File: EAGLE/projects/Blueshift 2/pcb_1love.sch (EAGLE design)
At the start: 20 parts, among them X1 RASPI_BOARD_B+_F

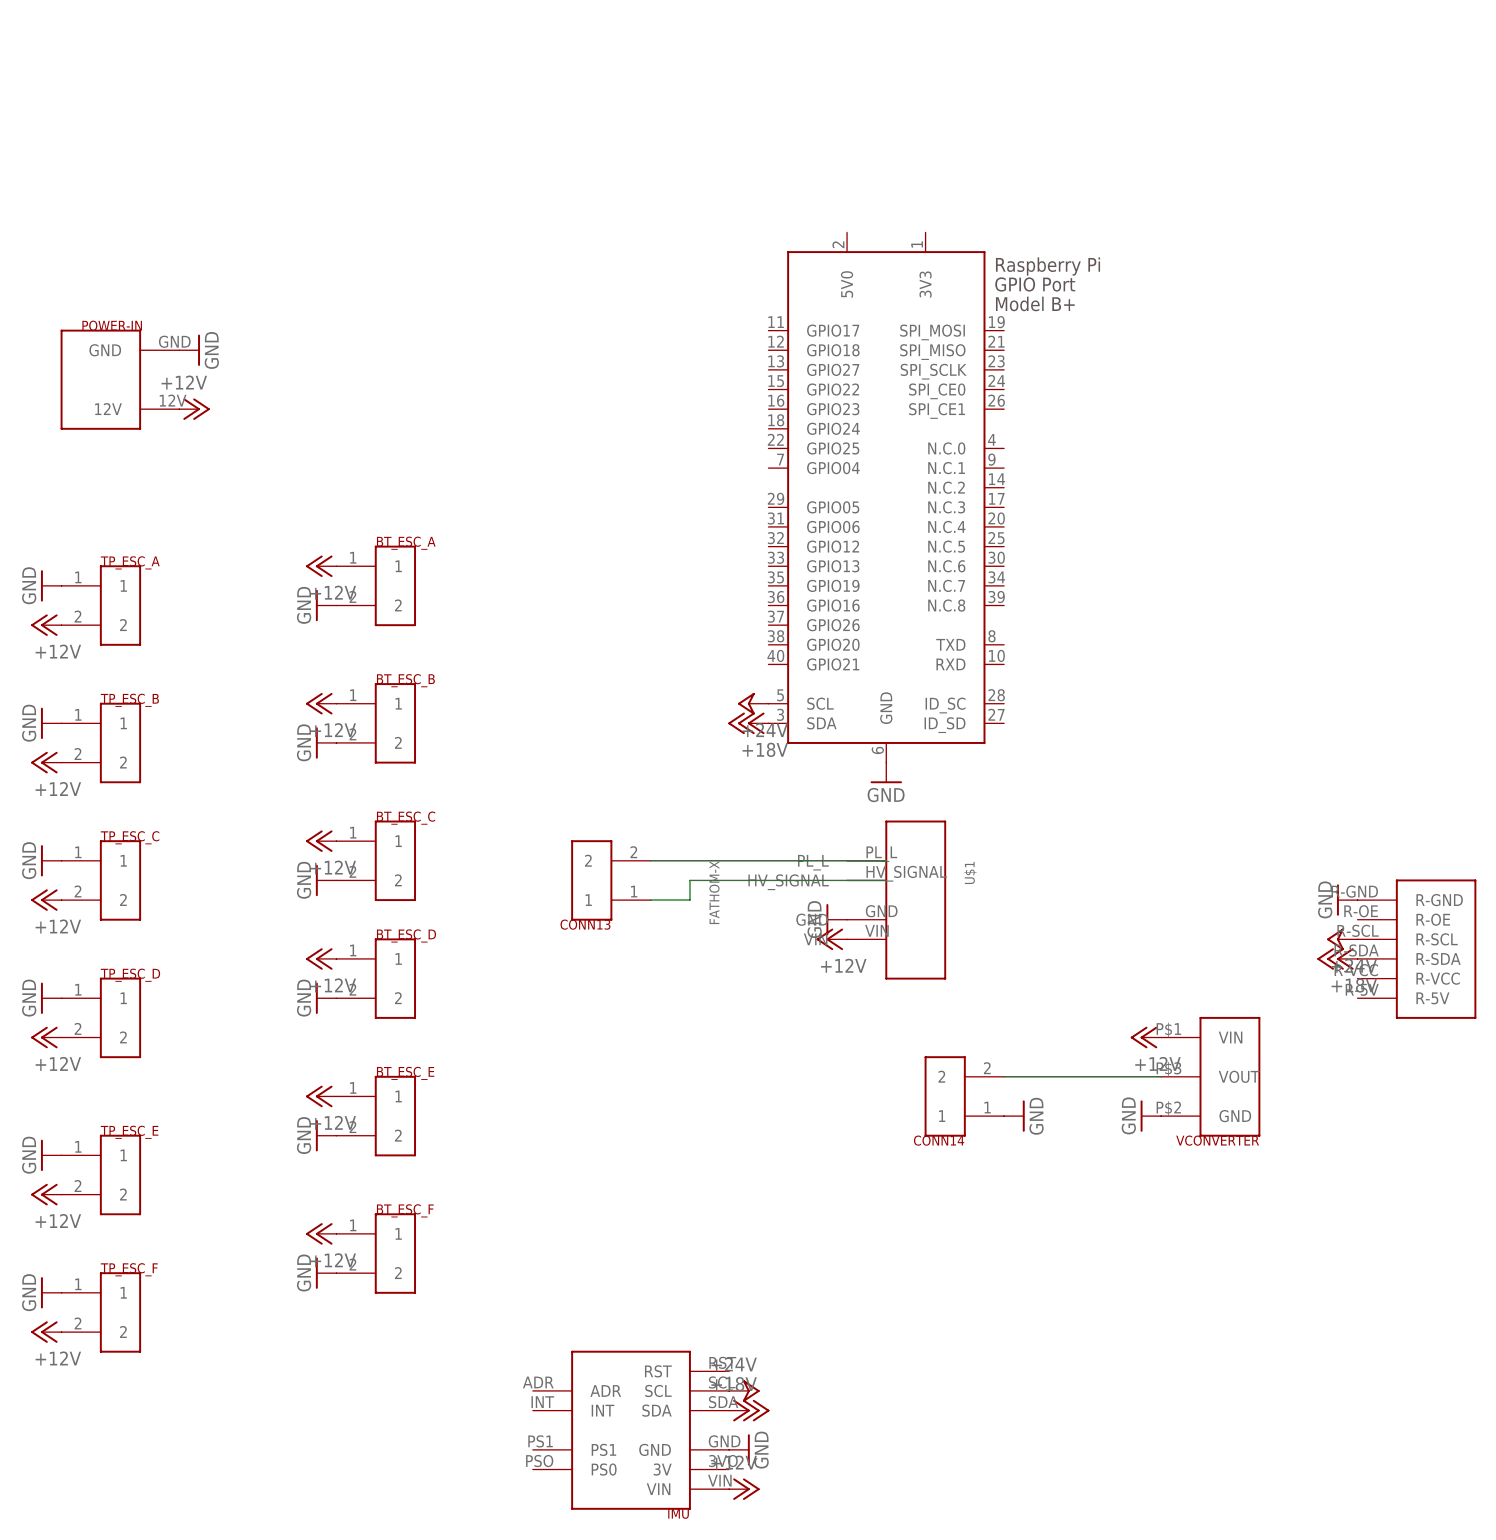
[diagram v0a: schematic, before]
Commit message: Fix power to IMU and PWM, RasPi cutout
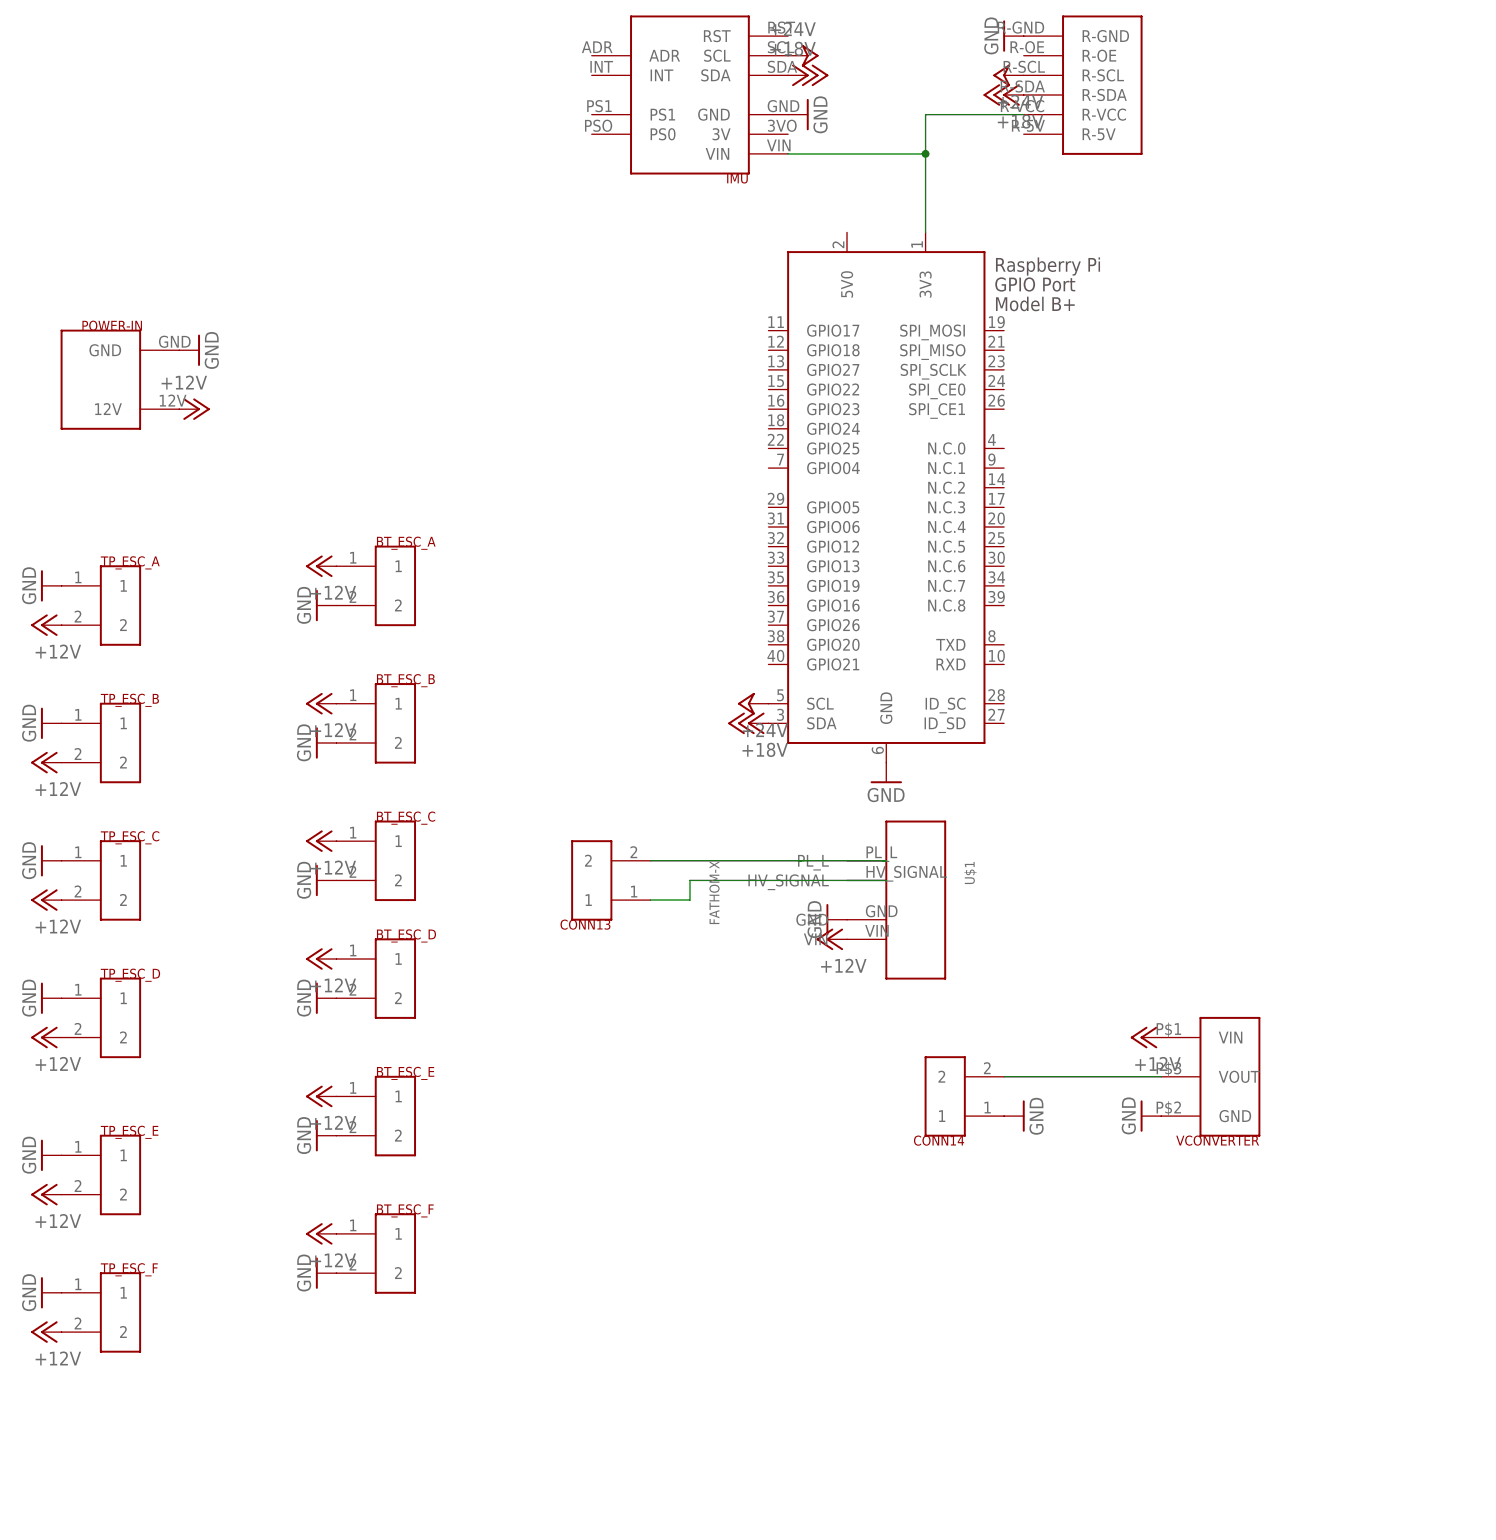
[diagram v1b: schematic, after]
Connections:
- new net N$4: IMU.VIN, PWM_EXT.R-VCC, X1.3V3
- net +12V: no longer IMU.VIN
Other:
- moved on the sheet: IMU
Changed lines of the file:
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@@
 <?xml version="1.0" encoding="utf-8"?>
 <!DOCTYPE eagle SYSTEM "eagle.dtd">
-<eagle version="9.5.2">
+<eagle version="9.6.0">
 <drawing>
 <settings>
@@
 <part name="GND18" library="supply1" library_urn="urn:adsk.eagle:library:371" deviceset="GND" device=""/>
 <part name="CONN14" library="BlueShift" deviceset="2CONTACT_ULTRAFIT_R/A" device=""/>
-<part name="P+20" library="supply1" library_urn="urn:adsk.eagle:library:371" deviceset="+12V" device=""/>
 <part name="GND19" library="supply1" library_urn="urn:adsk.eagle:library:371" deviceset="GND" device=""/>
 <part name="P+21" library="supply1" library_urn="urn:adsk.eagle:library:371" deviceset="+12V" device=""/>
@@
 </plain>
 <instances>
-<instance part="PWM_EXT" gate="G$1" x="106.68" y="55.88" smashed="yes"/>
-<instance part="IMU" gate="G$1" x="0" y="0" smashed="yes" rot="R180">
-<attribute name="NAME" x="7.62" y="-10.16" size="1.27" layer="94" rot="R180"/>
-<attribute name="VALUE" x="-7.62" y="10.16" size="1.27" layer="94"/>
+<instance part="PWM_EXT" gate="G$1" x="63.5" y="167.64" smashed="yes"/>
+<instance part="IMU" gate="G$1" x="7.62" y="172.72" smashed="yes" rot="R180">
+<attribute name="NAME" x="15.24" y="162.56" size="1.27" layer="94" rot="R180"/>
+<attribute name="VALUE" x="0" y="182.88" size="1.27" layer="94"/>
 </instance>
 <instance part="VCONVERTER" gate="G$1" x="78.74" y="45.72" smashed="yes">
@@
 <attribute name="VALUE" x="30.48" y="81.28" size="1.778" layer="96"/>
 </instance>
-<instance part="P+14" gate="1" x="15.24" y="5.08" smashed="yes" rot="R270">
-<attribute name="VALUE" x="10.16" y="7.62" size="1.778" layer="96"/>
+<instance part="P+14" gate="1" x="22.86" y="177.8" smashed="yes" rot="R270">
+<attribute name="VALUE" x="17.78" y="180.34" size="1.778" layer="96"/>
 </instance>
 <instance part="P+15" gate="1" x="15.24" y="93.98" smashed="yes" rot="R90">
 <attribute name="VALUE" x="20.32" y="91.44" size="1.778" layer="96" rot="R180"/>
 </instance>
-<instance part="P+16" gate="1" x="91.44" y="63.5" smashed="yes" rot="R90">
-<attribute name="VALUE" x="96.52" y="60.96" size="1.778" layer="96" rot="R180"/>
+<instance part="P+16" gate="1" x="48.26" y="175.26" smashed="yes" rot="R90">
+<attribute name="VALUE" x="53.34" y="172.72" size="1.778" layer="96" rot="R180"/>
 </instance>
 <instance part="P+17" gate="1" x="15.24" y="91.44" smashed="yes" rot="R90">
 <attribute name="VALUE" x="20.32" y="88.9" size="1.778" layer="96" rot="R180"/>
 </instance>
-<instance part="P+18" gate="1" x="15.24" y="2.54" smashed="yes" rot="R270">
-<attribute name="VALUE" x="10.16" y="5.08" size="1.778" layer="96"/>
-</instance>
-<instance part="P+19" gate="1" x="91.44" y="60.96" smashed="yes" rot="R90">
-<attribute name="VALUE" x="96.52" y="58.42" size="1.778" layer="96" rot="R180"/>
-</instance>
-<instance part="GND17" gate="1" x="15.24" y="-2.54" smashed="yes" rot="R90">
-<attribute name="VALUE" x="17.78" y="-5.08" size="1.778" layer="96" rot="R90"/>
-</instance>
-<instance part="GND18" gate="1" x="91.44" y="68.58" smashed="yes" rot="R270">
-<attribute name="VALUE" x="88.9" y="71.12" size="1.778" layer="96" rot="R270"/>
+<instance part="P+18" gate="1" x="22.86" y="175.26" smashed="yes" rot="R270">
+<attribute name="VALUE" x="17.78" y="177.8" size="1.778" layer="96"/>
+</instance>
+<instance part="P+19" gate="1" x="48.26" y="172.72" smashed="yes" rot="R90">
+<attribute name="VALUE" x="53.34" y="170.18" size="1.778" layer="96" rot="R180"/>
+</instance>
+<instance part="GND17" gate="1" x="22.86" y="170.18" smashed="yes" rot="R90">
+<attribute name="VALUE" x="25.4" y="167.64" size="1.778" layer="96" rot="R90"/>
+</instance>
+<instance part="GND18" gate="1" x="48.26" y="180.34" smashed="yes" rot="R270">
+<attribute name="VALUE" x="45.72" y="182.88" size="1.778" layer="96" rot="R270"/>
 </instance>
 <instance part="CONN14" gate="G$1" x="40.64" y="43.18" smashed="yes" rot="R180">
 <attribute name="NAME" x="43.18" y="38.1" size="1.27" layer="94" rot="R180"/>
 <attribute name="VALUE" x="38.1" y="40.64" size="1.27" layer="94" rot="R90"/>
-</instance>
-<instance part="P+20" gate="1" x="15.24" y="-7.62" smashed="yes" rot="R270">
-<attribute name="VALUE" x="10.16" y="-5.08" size="1.778" layer="96"/>
 </instance>
 <instance part="GND19" gate="1" x="50.8" y="40.64" smashed="yes" rot="R90">
@@
 </segment>
 <segment>
-<pinref part="P+20" gate="1" pin="+12V"/>
-<pinref part="IMU" gate="G$1" pin="VIN"/>
-</segment>
-<segment>
 <pinref part="P+21" gate="1" pin="+12V"/>
 <pinref part="VCONVERTER" gate="G$1" pin="VIN"/>
@@
 </segment>
 </net>
+<net name="N$4" class="0">
+<segment>
+<pinref part="X1" gate="G$1" pin="3V3"/>
+<pinref part="PWM_EXT" gate="G$1" pin="R-VCC"/>
+<wire x1="38.1" y1="154.94" x2="38.1" y2="165.1" width="0.1524" layer="91"/>
+<wire x1="38.1" y1="165.1" x2="38.1" y2="170.18" width="0.1524" layer="91"/>
+<wire x1="38.1" y1="170.18" x2="50.8" y2="170.18" width="0.1524" layer="91"/>
+<pinref part="IMU" gate="G$1" pin="VIN"/>
+<wire x1="20.32" y1="165.1" x2="38.1" y2="165.1" width="0.1524" layer="91"/>
+<junction x="38.1" y="165.1"/>
+</segment>
+</net>
